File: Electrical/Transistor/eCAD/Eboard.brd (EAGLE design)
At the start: 71.3 x 54.1 mm, 22 parts

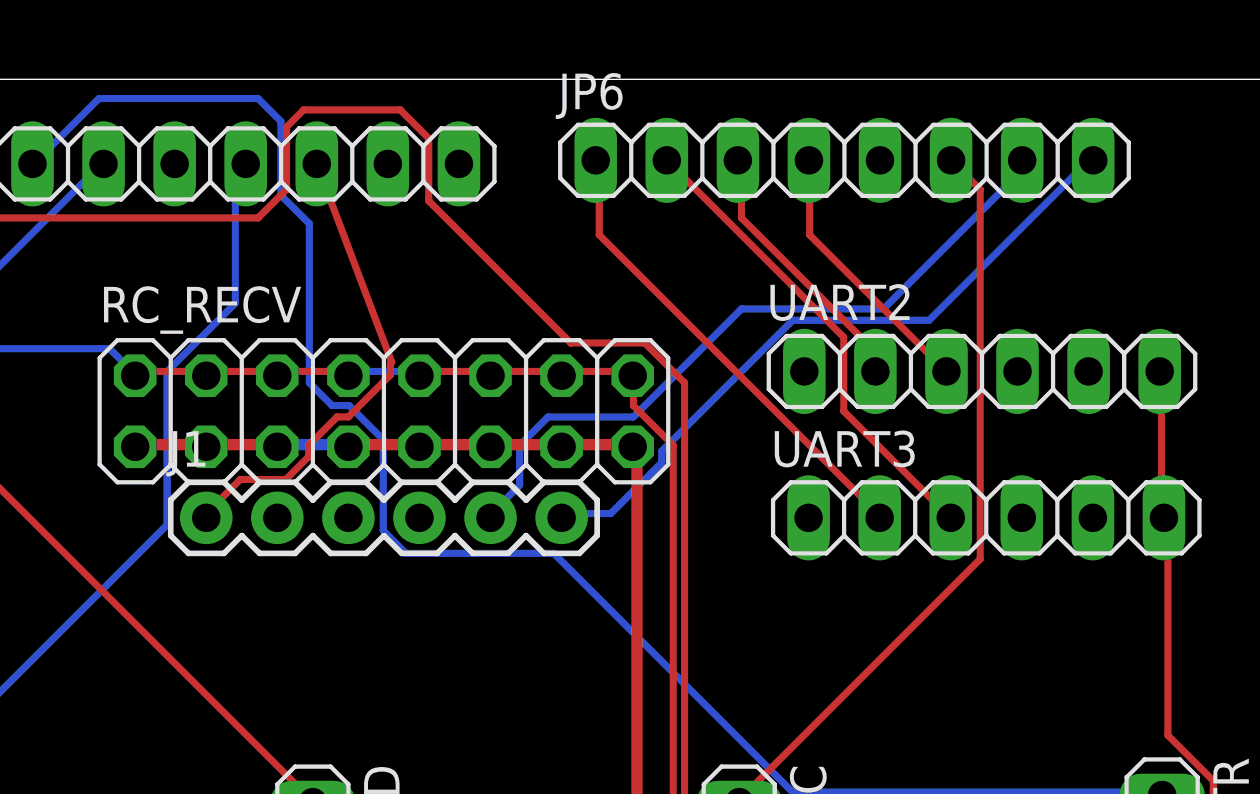
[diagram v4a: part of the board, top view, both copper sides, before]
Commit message: reversed J1 180 degrees
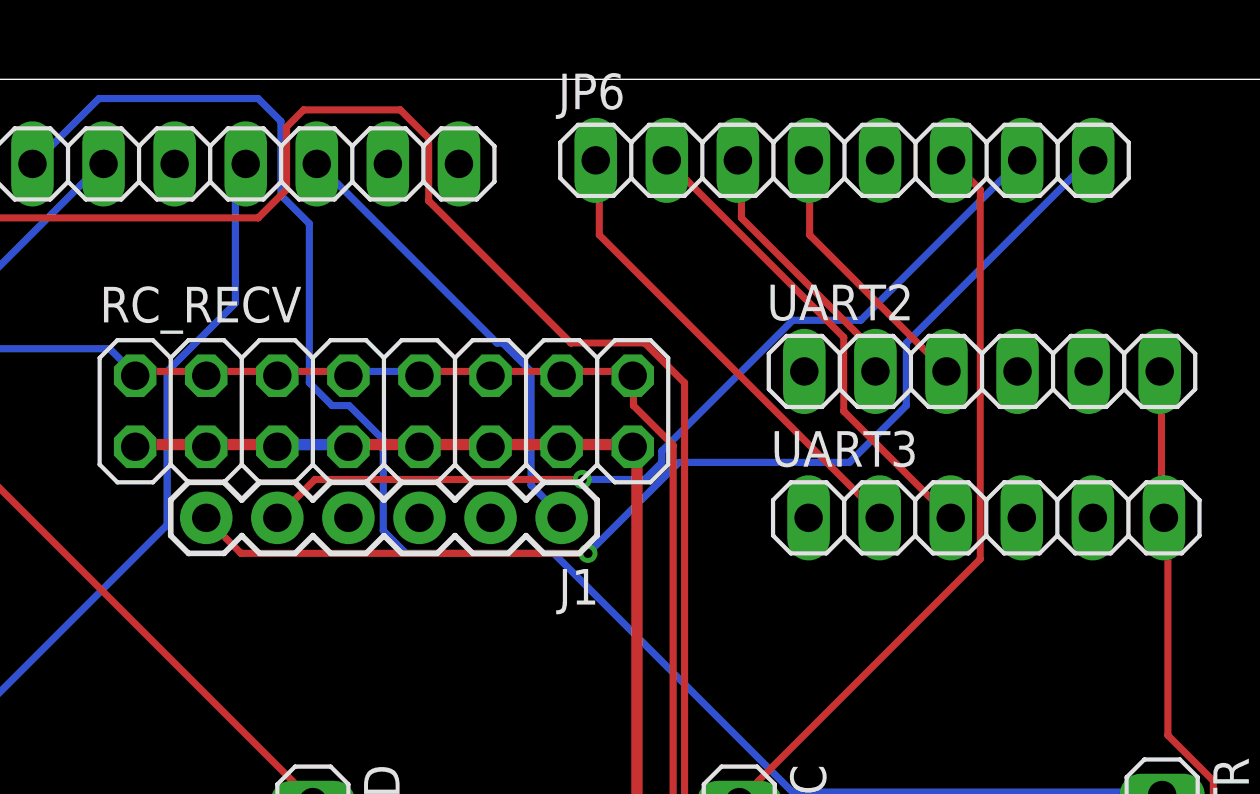
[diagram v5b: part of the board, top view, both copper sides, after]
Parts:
- moved J1 12.7 mm to (48.4, 83.2), turned to 180 degrees
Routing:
- net BRAKE_RC: track 24.5 -> 39.4 mm, vias 0 -> 1
- net AUTON_RC: track 25.4 -> 32.2 mm, vias 0 -> 1
- net STEERING_RC: track 17.1 -> 16.4 mm
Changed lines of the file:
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@@
 <element name="D1" library="SparkFun-LED" library_urn="urn:adsk.eagle:library:529" package="LED-1206" package3d_urn="urn:adsk.eagle:package:39352/1" value="" x="25.5778" y="57.7596"/>
 <element name="DIST_ENC" library="pinhead" package="1X03" value="" x="54.7878" y="70.4596" rot="R270"/>
-<element name="J1" library="SparkFun-Connectors" package="1X06" value="" x="35.7378" y="83.1596">
-<attribute name="PROD_ID" value="CONN-08437" x="35.7378" y="83.1596" size="1.778" layer="27" display="off"/>
+<element name="J1" library="SparkFun-Connectors" package="1X06" value="" x="48.4378" y="83.1596" rot="R180">
+<attribute name="PROD_ID" value="CONN-08437" x="48.4378" y="83.1596" size="1.778" layer="27" rot="R180" display="off"/>
 </element>
 <element name="JP1" library="pinhead" package="1X06" value="" x="17.8054" y="47.6631" rot="R180"/>
@@
 <contactref element="JP5" pad="6"/>
 <contactref element="J1" pad="1"/>
-<wire x1="40.4114" y1="86.7664" x2="40.8178" y2="86.7664" width="0.254" layer="1"/>
-<wire x1="39.3954" y1="85.7504" x2="40.4114" y2="86.7664" width="0.254" layer="1"/>
-<wire x1="39.3954" y1="85.344" x2="39.3954" y2="85.7504" width="0.254" layer="1"/>
-<wire x1="38.5826" y1="84.5312" x2="39.3954" y2="85.344" width="0.254" layer="1"/>
-<wire x1="36.957" y1="84.5312" x2="38.5826" y2="84.5312" width="0.254" layer="1"/>
-<wire x1="35.7378" y1="83.312" x2="36.957" y2="84.5312" width="0.254" layer="1"/>
-<wire x1="35.7378" y1="83.312" x2="35.7378" y2="83.1596" width="0.254" layer="1"/>
-<wire x1="42.3164" y1="88.265" x2="42.3164" y2="88.6709625" width="0.254" layer="1"/>
-<wire x1="42.3164" y1="88.6709625" x2="42.3672" y2="88.7217625" width="0.254" layer="1"/>
-<wire x1="42.3672" y1="88.7217625" x2="39.6875" y2="95.8088" width="0.254" layer="1"/>
-<wire x1="40.8178" y1="86.7664" x2="42.3164" y2="88.265" width="0.254" layer="1"/>
+<wire x1="46.1264" y1="89.408" x2="39.8272" y2="95.7072" width="0.254" layer="16"/>
+<wire x1="46.3296" y1="89.408" x2="46.1264" y2="89.408" width="0.254" layer="16"/>
+<wire x1="47.3456" y1="88.392" x2="46.3296" y2="89.408" width="0.254" layer="16"/>
+<wire x1="47.3456" y1="84.328" x2="47.3456" y2="88.392" width="0.254" layer="16"/>
+<wire x1="48.3616" y1="83.312" x2="47.3456" y2="84.328" width="0.254" layer="16"/>
+<wire x1="39.8272" y1="95.7072" x2="39.6875" y2="95.8088" width="0.254" layer="16"/>
+<wire x1="48.3616" y1="83.312" x2="48.4378" y2="83.1596" width="0.254" layer="16"/>
 </signal>
 <signal name="BRAKE_RC">
 <contactref element="JP6" pad="8"/>
 <contactref element="J1" pad="6"/>
-<wire x1="61.5696" y1="90.2208" x2="67.2592" y2="95.9104" width="0.254" layer="16"/>
-<wire x1="56.6928" y1="90.2208" x2="61.5696" y2="90.2208" width="0.254" layer="16"/>
-<wire x1="52.0192" y1="85.5472" x2="56.6928" y2="90.2208" width="0.254" layer="16"/>
-<wire x1="52.0192" y1="85.1408" x2="52.0192" y2="85.5472" width="0.254" layer="16"/>
-<wire x1="50.1904" y1="83.312" x2="52.0192" y2="85.1408" width="0.254" layer="16"/>
-<wire x1="48.5648" y1="83.312" x2="50.1904" y2="83.312" width="0.254" layer="16"/>
+<wire x1="60.7568" y1="89.408" x2="67.2592" y2="95.9104" width="0.254" layer="16"/>
+<wire x1="60.7568" y1="87.1728" x2="60.7568" y2="89.408" width="0.254" layer="16"/>
+<wire x1="58.7248" y1="85.1408" x2="60.7568" y2="87.1728" width="0.254" layer="16"/>
+<wire x1="52.6288" y1="85.1408" x2="58.7248" y2="85.1408" width="0.254" layer="16"/>
+<wire x1="49.3776" y1="81.8896" x2="52.6288" y2="85.1408" width="0.254" layer="16"/>
+<wire x1="36.9824" y1="81.8896" x2="49.3776" y2="81.8896" width="0.254" layer="1"/>
+<wire x1="35.7632" y1="83.1088" x2="36.9824" y2="81.8896" width="0.254" layer="1"/>
 <wire x1="67.2592" y1="95.9104" x2="67.437" y2="95.9358" width="0.254" layer="16"/>
-<wire x1="48.5648" y1="83.312" x2="48.4378" y2="83.1596" width="0.254" layer="16"/>
+<wire x1="35.7632" y1="83.1088" x2="35.7378" y2="83.1596" width="0.254" layer="1"/>
+<via x="49.3776" y="81.8896" extent="1-16" drill="0.3302"/>
 </signal>
 <signal name="AUTON_RC">
 <contactref element="J1" pad="5"/>
 <contactref element="JP6" pad="7"/>
-<wire x1="64.8208" y1="95.504" x2="64.8208" y2="95.9104" width="0.254" layer="16"/>
-<wire x1="59.944" y1="90.6272" x2="64.8208" y2="95.504" width="0.254" layer="16"/>
-<wire x1="54.864" y1="90.6272" x2="59.944" y2="90.6272" width="0.254" layer="16"/>
-<wire x1="51.0032" y1="86.7664" x2="54.864" y2="90.6272" width="0.254" layer="16"/>
-<wire x1="47.9552" y1="86.7664" x2="51.0032" y2="86.7664" width="0.254" layer="16"/>
-<wire x1="46.9392" y1="85.7504" x2="47.9552" y2="86.7664" width="0.254" layer="16"/>
-<wire x1="46.9392" y1="84.328" x2="46.9392" y2="85.7504" width="0.254" layer="16"/>
-<wire x1="45.9232" y1="83.312" x2="46.9392" y2="84.328" width="0.254" layer="16"/>
+<wire x1="59.1312" y1="90.2208" x2="64.8208" y2="95.9104" width="0.254" layer="16"/>
+<wire x1="56.6928" y1="90.2208" x2="59.1312" y2="90.2208" width="0.254" layer="16"/>
+<wire x1="52.0192" y1="85.5472" x2="56.6928" y2="90.2208" width="0.254" layer="16"/>
+<wire x1="52.0192" y1="85.1408" x2="52.0192" y2="85.5472" width="0.254" layer="16"/>
+<wire x1="51.4096" y1="84.5312" x2="52.0192" y2="85.1408" width="0.254" layer="16"/>
+<wire x1="49.1744" y1="84.5312" x2="51.4096" y2="84.5312" width="0.254" layer="16"/>
+<wire x1="39.624" y1="84.5312" x2="49.1744" y2="84.5312" width="0.254" layer="1"/>
+<wire x1="38.4048" y1="83.312" x2="39.624" y2="84.5312" width="0.254" layer="1"/>
 <wire x1="64.8208" y1="95.9104" x2="64.897" y2="95.9358" width="0.254" layer="16"/>
-<wire x1="45.9232" y1="83.312" x2="45.8978" y2="83.1596" width="0.254" layer="16"/>
+<wire x1="38.4048" y1="83.312" x2="38.2778" y2="83.1596" width="0.254" layer="1"/>
+<via x="49.1744" y="84.5312" extent="1-16" drill="0.3302"/>
 </signal>
 <signal name="N$1">

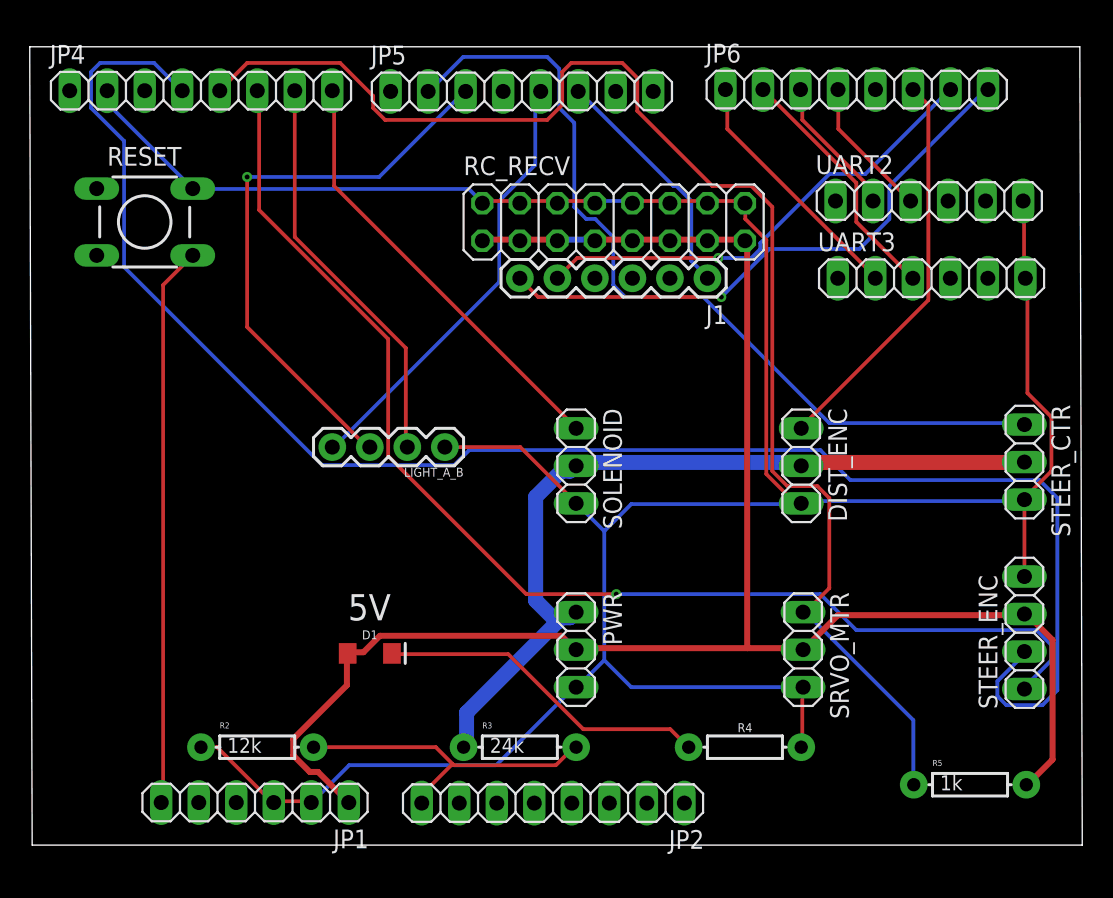
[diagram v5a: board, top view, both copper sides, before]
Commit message: reversed steering pins to match configuration of existing connector
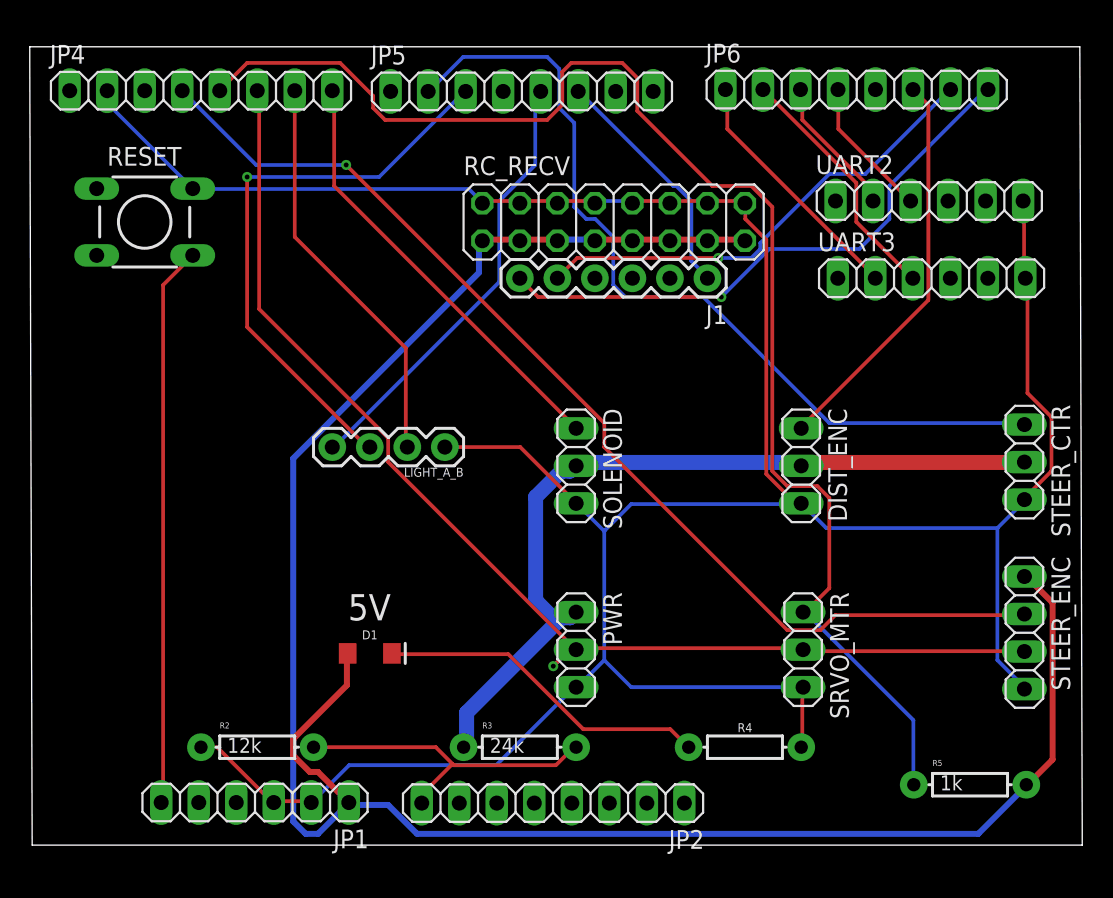
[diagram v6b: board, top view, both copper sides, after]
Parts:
- turned STEER_ENC to 270 degrees
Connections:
- net STEER_ENC2 renamed STEER_ENCB
- removed net STEER_ENC1: JP4.6, STEER_ENC.1
- new net STEER_ENCA: JP4.6, PWR.2, SRVO_MTR.2, STEER_ENC.3
- net 5V: now also STEER_ENC.1; no longer PWR.2, SRVO_MTR.2, STEER_ENC.3
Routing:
- net STEER_ENC1: track 82.3 -> 0.00 mm, vias 1 -> 0
- net STEER_ENCA: track 0.00 -> 80.2 mm, vias 0 -> 1
- net STEER_ENCB: track 113.4 -> 73.6 mm, vias 0 -> 1
- net 5V: track 120.9 -> 145.9 mm
- net GND: track 200.0 -> 207.8 mm

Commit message: checked to see if trace connections in schematic were sensical, added ground and 5V symbols to schematic for readability, checked alignment of pin sets in board file for alignment, rerouted board file based on amendments in schematic, checked that 12V traces were 40 mils, 5V traces were 16 mils, and all other traces (incl. VBATT_ADC) were 10 mils
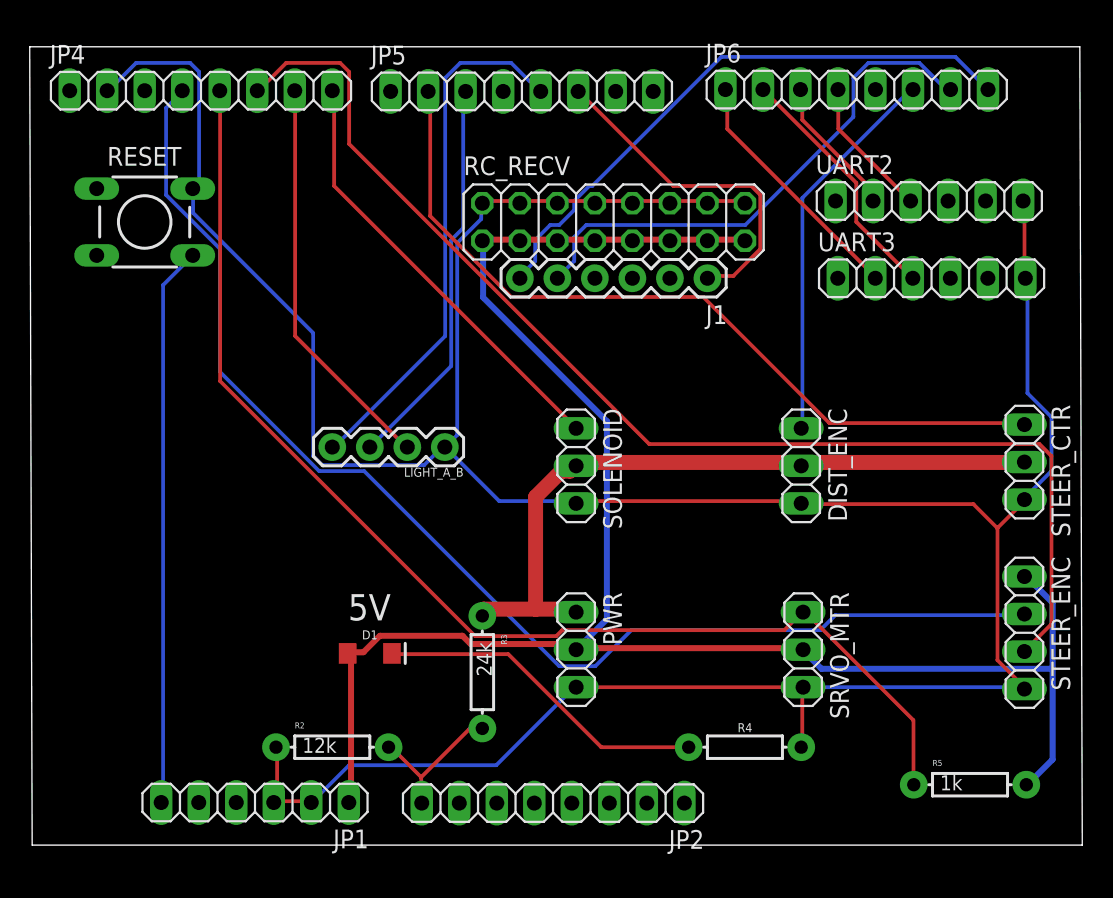
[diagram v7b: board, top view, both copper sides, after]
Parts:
- moved R3 5.68 mm to (33.2, 56.5), turned to 270 degrees
- moved R2 5.08 mm to (23.0, 51.4)
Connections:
- net LIGHT_1 renamed LIGHT_GREEN
- net LIGHT_2 renamed LIGHT_BLUE
- net LIGHT_3 renamed LIGHT_RED
- net 5V: now also PWR.2, SRVO_MTR.2
- net STEER_ENCA: no longer PWR.2, SRVO_MTR.2
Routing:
- net 5V: track 145.9 -> 125.4 mm
- net GND: track 207.8 -> 221.4 mm
- net SRVO_MTR: track 94.5 -> 81.8 mm
- net LIGHT_BLUE: track 39.0 -> 26.8 mm, vias 1 -> 0
- net VBATT_ADC: track 22.3 -> 10.3 mm
- net STEER_ENCB: track 73.6 -> 85.2 mm, vias 1 -> 0
- net 12V: track 56.1 -> 48.6 mm
- net STEERING_RC: track 16.4 -> 23.3 mm
- net LIGHT_GREEN: track 30.1 -> 35.9 mm
- net STEER_CTR: track 58.5 -> 54.6 mm
- net AUTON_RC: track 32.2 -> 36.0 mm, vias 1 -> 0
- net STEER_ENCA: track 80.2 -> 82.4 mm, vias 1 -> 0
- net DIST_ENC: track 26.9 -> 26.1 mm
- net BRAKE_RC: track 39.4 -> 40.1 mm, vias 1 -> 0
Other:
- board text added: "ROBOBUGGY REV 1.8"
- board text removed: "ROBOBUGGY REV 1.7"

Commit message: updated the light names, updated the offset on shield to match arduino mega to resolve alignment issues in 1.7, updated silkscreen with labels for pins, added dimensions to tDocu layer in inches, double checked pins match on shield, checked that orientations for all pins were correct on board
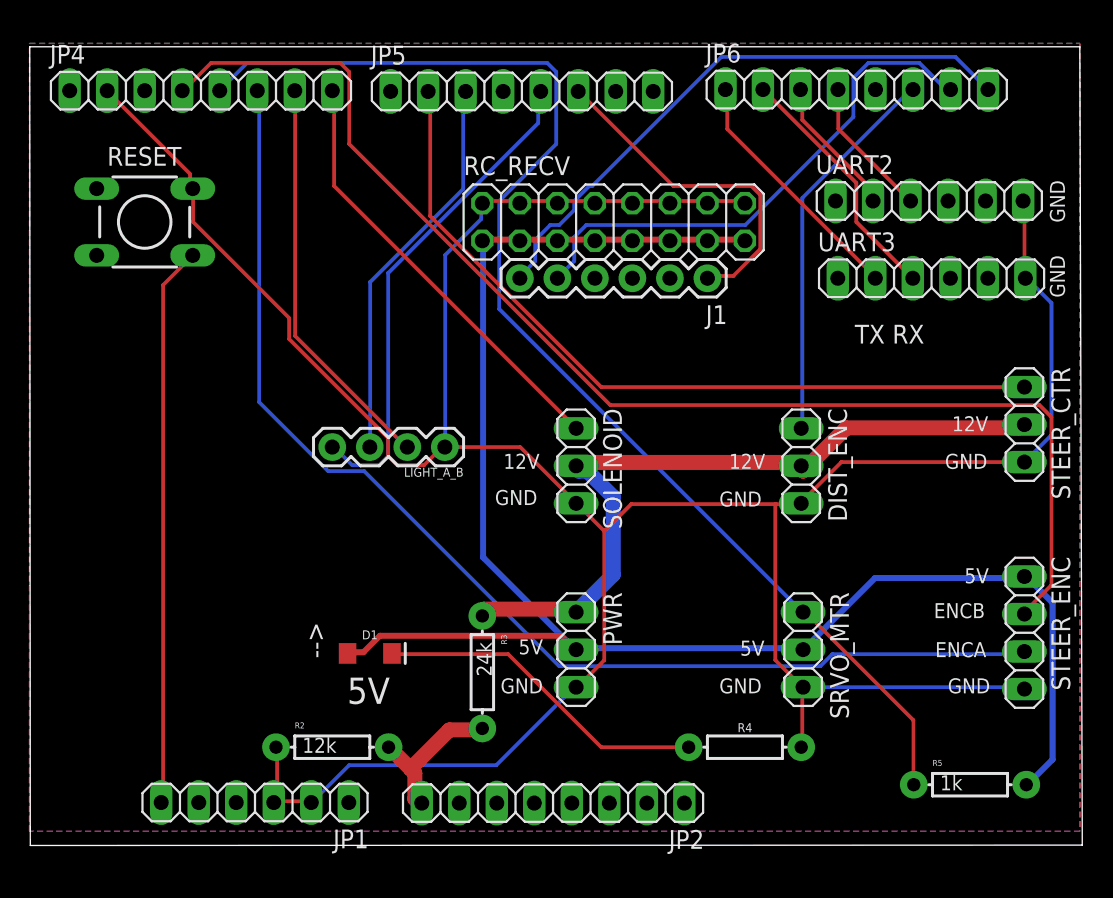
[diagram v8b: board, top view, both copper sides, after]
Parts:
- moved STEER_CTR 2.54 mm to (69.9, 73.3)
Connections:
- net 5V: no longer JP1.1
- net LIGHT_BLUE: now also JP5.5, LIGHT_A_B.4; no longer JP5.3, LIGHT_A_B.3
- net LIGHT_GREEN: now also JP5.3, LIGHT_A_B.3; no longer JP5.5, LIGHT_A_B.4
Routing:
- net GND: track 221.4 -> 208.3 mm
- net 5V: track 125.4 -> 113.4 mm
- net LIGHT_GREEN: track 35.9 -> 26.8 mm
- net LIGHT_BLUE: track 26.8 -> 33.5 mm
- net SRVO_MTR: track 81.8 -> 85.4 mm
- net 12V: track 48.6 -> 51.1 mm
- net STEER_ENCA: track 82.4 -> 80.9 mm
- net STEER_ENCB: track 85.2 -> 86.5 mm
- net STEER_CTR: track 54.6 -> 53.5 mm
- added copper zone on layer 1, net N$2
- added copper zone on layer 16, net N$3
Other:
- outline, holes or cut-outs redrawn
- board text added: "-->"
- board text added: "12V"
- board text added: "BLUE"
- board text added: "ENCA"
- board text added: "ENCB"
- board text added: "GND"
- board text added: "GREEN"
- board text added: "RED"
- board text added: "RX"
- board text added: "TX"
